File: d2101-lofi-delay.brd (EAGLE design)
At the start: 100 x 50 mm, 65 parts, among them U3 FX2-20P-1.27DS, U4 FX2-20S-1.27DS

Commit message: D2101 done
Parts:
- removed C10, C11, C8, C9: 100N, capacitors:C-0805
- removed C12: 100N(FILM), capacitors:C050-025X075
- removed C13: 10N(FILM), capacitors:C050-025X075
- removed DA3, DA4: NE5532, f-opamp:SO08
- removed DA5, DA6: NJM2068M, ic-jrc:SO-8
- removed R19: 1K, resistors:R-0805
- removed R20: 20K, resistors:R-0805
- removed R21, R24, R25: 100K, resistors:R-0805
- removed R22, R23: 2*B50K*, potentiometers:RV11-DUAL
- added C23: 47U/16V, capacitors-electrolytic:E2-5
- added C27, C32, C33: 100N(FILM), capacitors:C050-025X075
- added C28, C29: 10N(FILM), capacitors:C050-025X075
- added C30, C31, C34, C35: 100N, capacitors:C-0805
- added C36, C37: 47N(FILM), capacitors:C050-025X075
- added C38, C39: 47U/35V, capacitors-electrolytic:E3,5-8
- added DD2: PT2399S, ic-princeton-technologies:SO-16
- added R29, R30, R31, R34, R35, R36, R37, R38, R39: 10K, resistors:R-0805
- added R32, R33: 15K, resistors:R-0805
- added R40, R42: 2*B50K*, potentiometers:RV11-DUAL
- added R41, R43, R44, R45: 1K, resistors:R-0805
- added SA2: 108-0051-EVX, switches:108-0051-EVX
- added VD1, VD2, VD3, VD4: BAV199, diodes:SOT23
- C16, C17: value 2N2(FILM) -> 10N(FILM)
- C19: value 47U/16V -> 100N; device capacitors-electrolytic:E2-5 -> capacitors:C-0805
- C20, C21: value 100N -> 2N2(FILM); device capacitors:C-0805 -> capacitors:C050-025X075
- C22: value 10N(FILM) -> 47U/16V; device capacitors:C050-025X075 -> capacitors-electrolytic:E2-5
- C24: value 47N(FILM) -> 2N2(FILM)
- C25: value 10U/35V -> 2N2(FILM); device capacitors-electrolytic:E2-5 -> capacitors:C050-025X075
- C26: value 22P -> 100N(FILM); device capacitors:C-0805 -> capacitors:C050-025X075
- DA1: value NE5532 -> NJM78L05UA; device f-opamp:SO08 -> regulators-linear:SOT89
- DA2: value NCP1117ST50T3G -> NJM2068M; device regulators-linear:SOT223 -> ic-jrc:SO-8
- R1: value 100K -> 10K
- R10: value 22K -> 10K
- R12, R14: value 10K -> 10R(1206); device resistors:R-0805 -> resistors:R-1206
- R13: value 1K -> 10R(1206); device resistors:R-0805 -> resistors:R-1206
- R15, R16: value 10K -> 15K
- R17: value 10K -> 1K
- R18: value 15K -> 1K
- R2: value 2*B20K(CD) -> 10K; device potentiometers:RV11-DUAL -> resistors:R-0805
- R26, R27: value 10K -> 100K
- R5: value 100K -> 2*B20K(CD); device resistors:R-0805 -> potentiometers:RV11-DUAL
- R6, R7, R8: value 10R(1206) -> 10K; device resistors:R-1206 -> resistors:R-0805
- R9: value 15K -> 10K
- SA1: value 108-0051-EVX -> 108-0052-EVX; device switches:108-0051-EVX -> switches:108-0052-EVX
- moved R28 353.6 mm to (50.5, 23.0), turned to 90 degrees
- moved C3 347.6 mm to (8.00, 29.8), turned to 90 degrees
- moved R26 347.2 mm to (48.0, 23.0), turned to 270 degrees
- moved R9 344.0 mm to (24.5, 22.0), turned to 90 degrees
- moved R27 339.8 mm to (45.5, 13.0), turned to 270 degrees
- moved R2 337.4 mm to (27.0, 13.0)
- moved R4 330.5 mm to (27.0, 18.0)
- moved SA1 329.1 mm to (17.0, 37.0), turned to 180 degrees
- moved C26 326.7 mm to (58.0, 30.0), turned to 180 degrees
- moved R3 325.6 mm to (27.0, 15.5), turned to 180 degrees
- moved C24 309.6 mm to (58.0, 27.0), turned to 180 degrees
- moved C22 303.0 mm to (71.0, 26.0)
- moved C25 302.8 mm to (58.0, 15.0)
- moved R18 289.7 mm to (34.0, 32.0)
- moved R14 282.7 mm to (35.0, 36.0), turned to 180 degrees
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- renumbered U3 to U1, U4 to U2
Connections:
- removed net N$12: C25.-, R20.1, R24.2
- removed net N$26: R1.1
- removed net N$27: R22.2'
- removed net N$29: C3.2, DA6.1, R9.2
- removed net N$66: R13.1, SA1.2
- removed net V+: DA5.8, DA6.8
- removed net V-: DA5.4, DA6.4
- new net FBK_INT_LEFT: C3.2, DA2.1, PCB1.BOUTL', R15.2, SA1.4
- new net FBK_INT_RIGHT: C4.2, DA2.7, PCB1.BOUTR', R16.2, SA1.1
- new net FBK_LEFT: PCB1.ALFBK, PCB1.ALFBK', SA1.6
- new net FBK_RIGHT: PCB1.ARFBK, PCB1.ARFBK', SA1.3
- new net N$39: DA2.5, R11.2, R8.2
- new net N$40: R10.2, R11.1, R5.1'
- new net N$48: C28.2, R34.2, R36.2, R38.2
- new net N$49: C20.1, DD1.16, R30.1
- new net N$50: C20.2, DD1.15, R32.1
- new net N$51: C24.1, DD1.14, R34.1, R44.1
- new net N$52: C24.2, DD1.13, R36.1
- new net N$53: C26.1, DD1.12, R38.1
- new net N$54: C26.2, DD1.11
- new net N$55: C32.1, DD1.10
- new net N$56: C32.2, DD1.9
- new net N$57: C36.2, C38.+, R44.2
- new net N$58: C30.2, DD1.7
- new net N$59: C34.2, DD1.8
- new net N$60: DD1.6, R41.2
- new net N$62: C14.2, R26.2, R28.1
- new net N$63: C16.2, R28.2, R30.2, R32.2
- new net N$69: C22.+, DD1.2
- new net OUT_LEFT: C39.-, R10.1
- new net OUT_RIGHT: C38.-, R3.1
- net +15V: now also DA2.8, R13.2; no longer C10.2, C8.2, DA1.8, DA3.8, DA4.8, R6.2
- net +5V: now also C19.2, DA1.1, DD2.1; no longer DA2.2, DA2.4
- net -15V: now also DA2.4, R14.2; no longer C11.1, C9.1, DA1.4, DA3.4, DA4.4, R8.2
- net GND: now also C16.1, C17.1, C19.1, C22.-, C23.-, C28.1, C29.1, C30.1, C31.1, C34.1, C35.1, C36.1, C37.1, DA1.2, DA1.2@1, DD2.3, DD2.4, R26.1, R27.1, R40.2, R40.3, R42.2, R42.2', R42.3, R42.3', R5.2, R5.2', R6.1, R9.1, VD1.1, VD2.2, VD3.1, VD4.2; no longer C10.1, C11.2, C13.1, C19.-, C20.1, C21.1, C22.1, C24.1, C8.1, C9.2, DA2.1, DA5.3, DA5.5, R2.2, R22.1', R22.2, R22.3, R23.2', R23.3', R24.1, R25.1, R3.1
- net N$1: now also R42.1, R43.1; no longer PCB1.ALFBK, PCB1.ALFBK'
- net N$10: now also C17.2, R29.2, R31.2, R33.2; no longer C13.2, R12.2, R14.2, R18.2
- net N$11: now also PCB1.BINL, R1.1; no longer R28.1
- net N$13: now also R18.1, SA1.2; no longer C26.1, DA5.6, R20.2, R21.1
- net N$14: now also R42.1', SA2.3; no longer R23.1', SA1.3
- net N$15: now also C29.2, R35.2, R37.2, R39.2; no longer C22.2, R15.2, R16.2, R17.2
- net N$17: now also C21.2, DD2.15, R33.1; no longer C16.2, DD1.15, R18.1
- net N$18: now also C25.1, DD2.14, R35.1, R45.1; no longer C17.1, DD1.14, R15.1, R19.1
- net N$19: now also C25.2, DD2.13, R37.1; no longer C17.2, DD1.13, R16.1
- net N$2: now also R41.1, SA2.2; no longer PCB1.ARFBK, PCB1.ARFBK'
- net N$20: now also C27.1, DD2.12, R39.1; no longer C14.1, DD1.12, R17.1
- net N$21: now also C27.2, DD2.11; no longer C14.2, DD1.11
- net N$22: now also C33.1, DD2.10; no longer C15.1, DD1.10
- net N$23: now also C33.2, DD2.9; no longer C15.2, DD1.9
- net N$24: now also C37.2, C39.+, R45.2; no longer C24.2, C25.+, R19.2
- net N$25: now also C4.1, DA2.6, R16.1, R9.2; no longer R5.1
- net N$28: now also PCB1.BINR, R7.1; no longer R4.1
- net N$3: now also C15.1, R17.2, VD1.2, VD2.1; no longer C4.1, DA5.2, R1.2, R10.1, R5.2
- net N$30: now also R1.2, R2.1, R5.3; no longer R2.3, R26.1, R4.2
- net N$31: now also C31.2, DD2.7; no longer C20.2, DD1.7
- net N$32: now also C35.2, DD2.8; no longer C21.2, DD1.8
- net N$33: now also DD2.6, R43.2; no longer DD1.6, R13.2
- net N$36: now also R14.1; no longer R8.1
- net N$37: now also C23.+, DD2.2; no longer C19.+, DD1.2
- net N$4: now also C21.1, DD2.16, R31.1; no longer C16.1, DD1.16, R14.1
- net N$44: now also DA1.3, R12.2; no longer DA2.3, R7.2
- net N$5: now also C14.1, R18.2, VD3.2, VD4.1; no longer C4.2, DA5.1, R10.2, R11.1
- net N$6: now also R17.1, SA1.5; no longer C12.1, R11.2
- net N$61: now also DA2.3, R2.2, R4.2; no longer DA6.3, R26.2, R27.2
- net N$64: now also DA2.2, R15.1, R6.2; no longer DA6.2, R3.2, R9.1
- net N$65: now also R3.2, R4.1, R5.1; no longer R2.1, R27.1, R28.2
- net N$7: now also R5.3', R7.2, R8.1; no longer C26.2, DA5.7, R21.2, R22.3'
- net N$8: now also R40.1, SA2.1; no longer R22.1, SA1.1
- net N$9: now also C15.2, R27.2, R29.1; no longer C12.2, R12.1, R25.2
- net P+15V: now also R12.1, R13.1; no longer R6.1, R7.1
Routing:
- net FBK_INT_RIGHT: track 0.00 -> 82.4 mm
- net N$44: track 0.00 -> 79.0 mm
- net +5V: track 0.00 -> 73.3 mm
- net FBK_LEFT: track 0.00 -> 72.5 mm
- net FBK_INT_LEFT: track 0.00 -> 63.3 mm
- net FBK_RIGHT: track 0.00 -> 58.1 mm
- net -15V: track 0.00 -> 53.3 mm
- net P+15V: track 0.00 -> 48.7 mm
- net N$16: track 0.00 -> 46.9 mm
- net N$36: track 0.00 -> 43.4 mm
- net OUT_LEFT: track 0.00 -> 41.4 mm
- net N$39: track 0.00 -> 40.7 mm, vias 0 -> 3
- net +15V: track 0.00 -> 38.8 mm, vias 0 -> 1
- net N$24: track 0.00 -> 35.9 mm
- net N$28: track 0.00 -> 33.0 mm
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
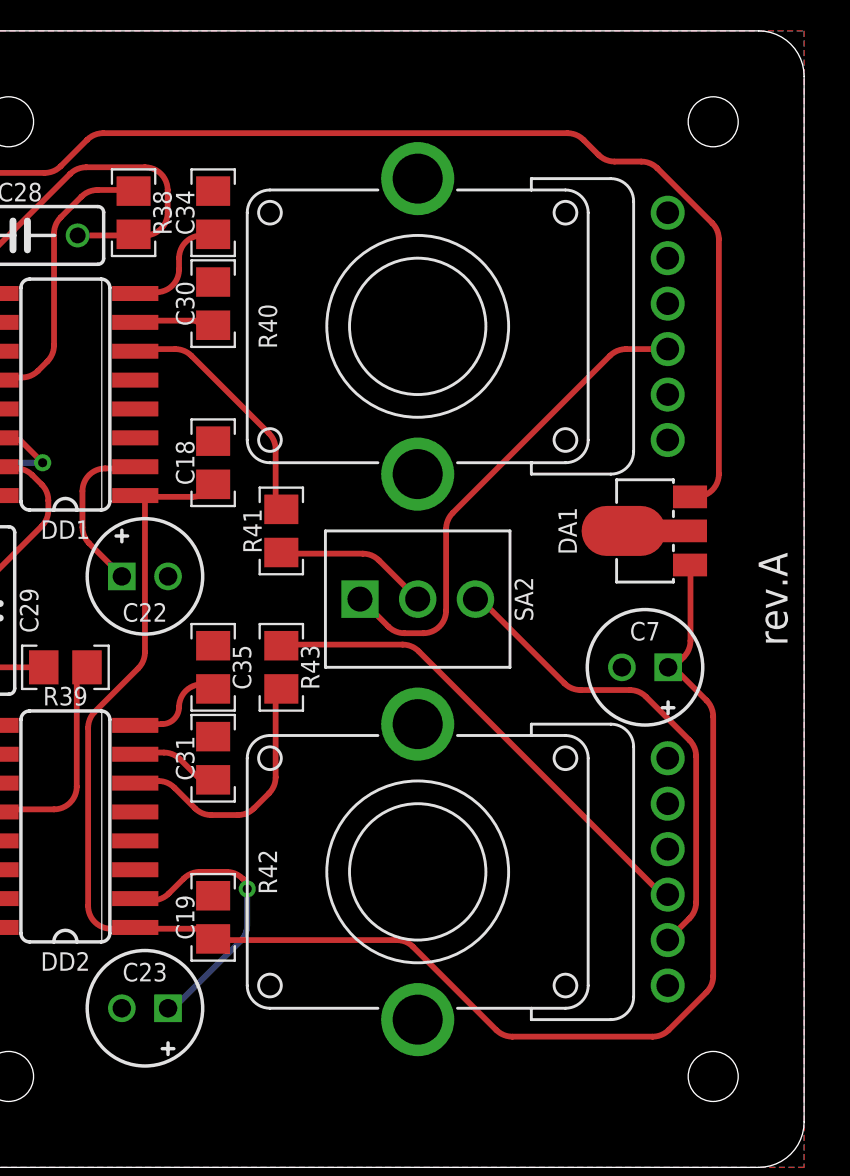
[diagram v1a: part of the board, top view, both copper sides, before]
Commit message: Replace switchable delay potentiometers with single ones
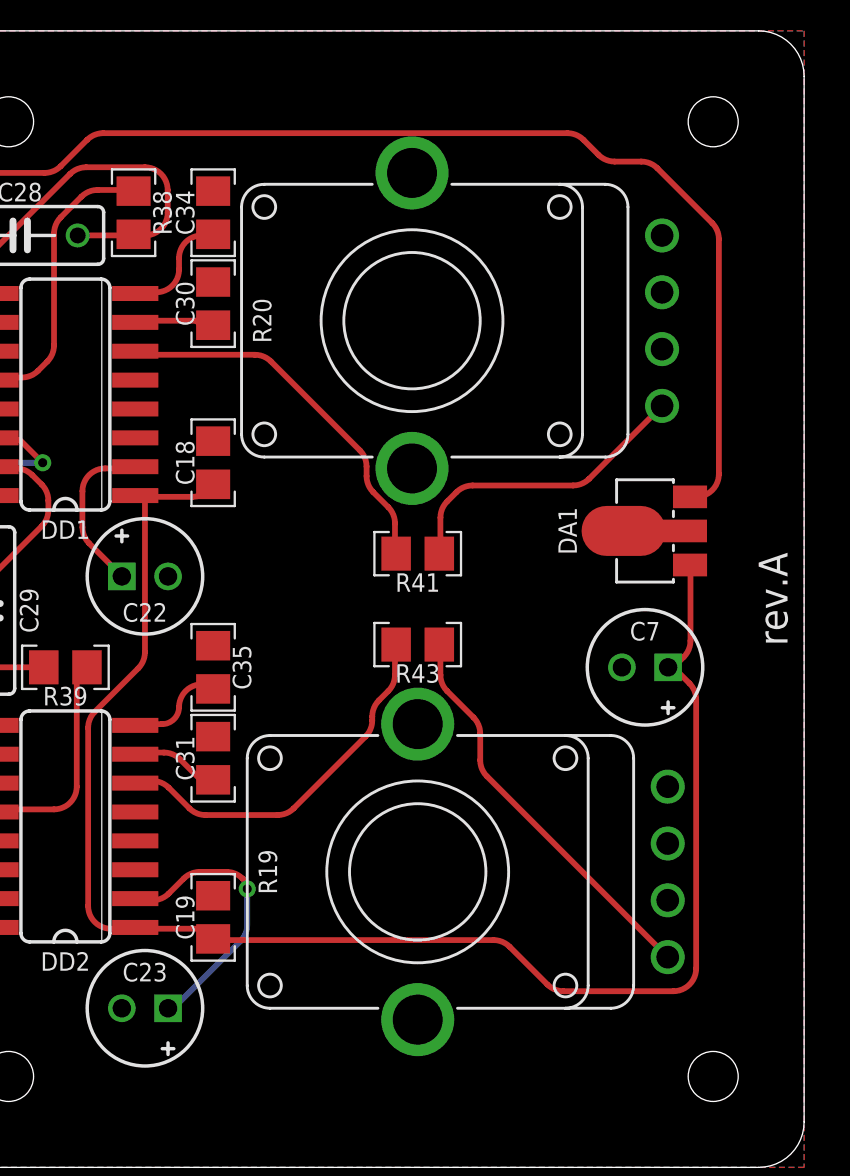
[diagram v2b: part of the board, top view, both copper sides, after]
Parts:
- removed R40, R42: 2*B50K*, potentiometers:RV11-DUAL
- removed SA2: 108-0051-EVX, switches:108-0051-EVX
- added R19, R20: B50K**, potentiometers:RV11-SINGLE
- moved R41 6.08 mm to (83.0, 27.0), turned to 180 degrees
- moved R43 6.08 mm to (83.0, 23.0), turned to 180 degrees
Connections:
- removed net N$14: R42.1', SA2.3
- removed net N$8: R40.1, SA2.1
- net GND: now also R19.2, R19.3, R20.2, R20.3; no longer R40.2, R40.3, R42.2, R42.2', R42.3, R42.3'
- net N$1: now also R19.1; no longer R42.1
- net N$2: now also R20.1; no longer SA2.2
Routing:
- net N$8: track 21.5 -> 0.00 mm
- net N$14: track 21.2 -> 0.00 mm
- net N$2: track 6.82 -> 13.5 mm
- net N$60: track 11.3 -> 16.7 mm
- net N$33: track 11.9 -> 16.5 mm
- net N$1: track 21.5 -> 17.8 mm
- net +5V: track 73.3 -> 70.2 mm

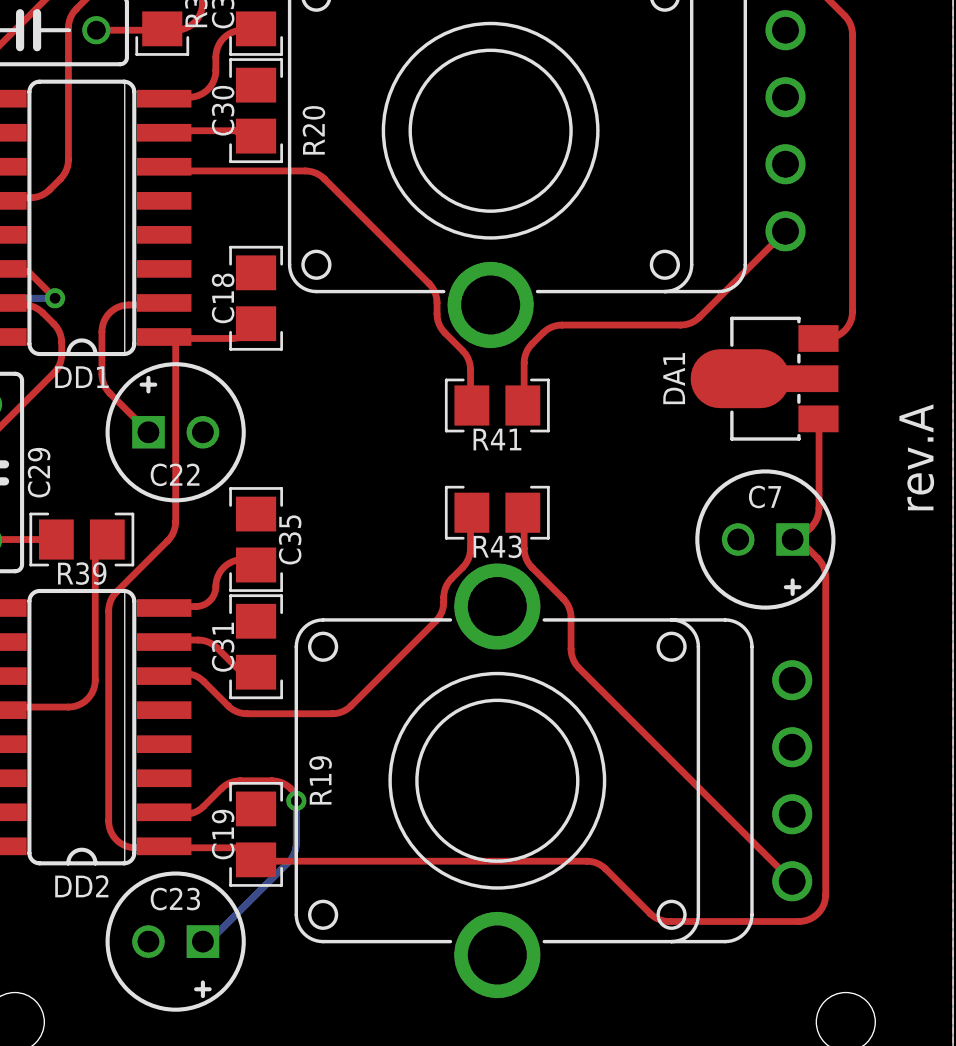
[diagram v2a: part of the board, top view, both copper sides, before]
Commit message: Minor routing adjustment
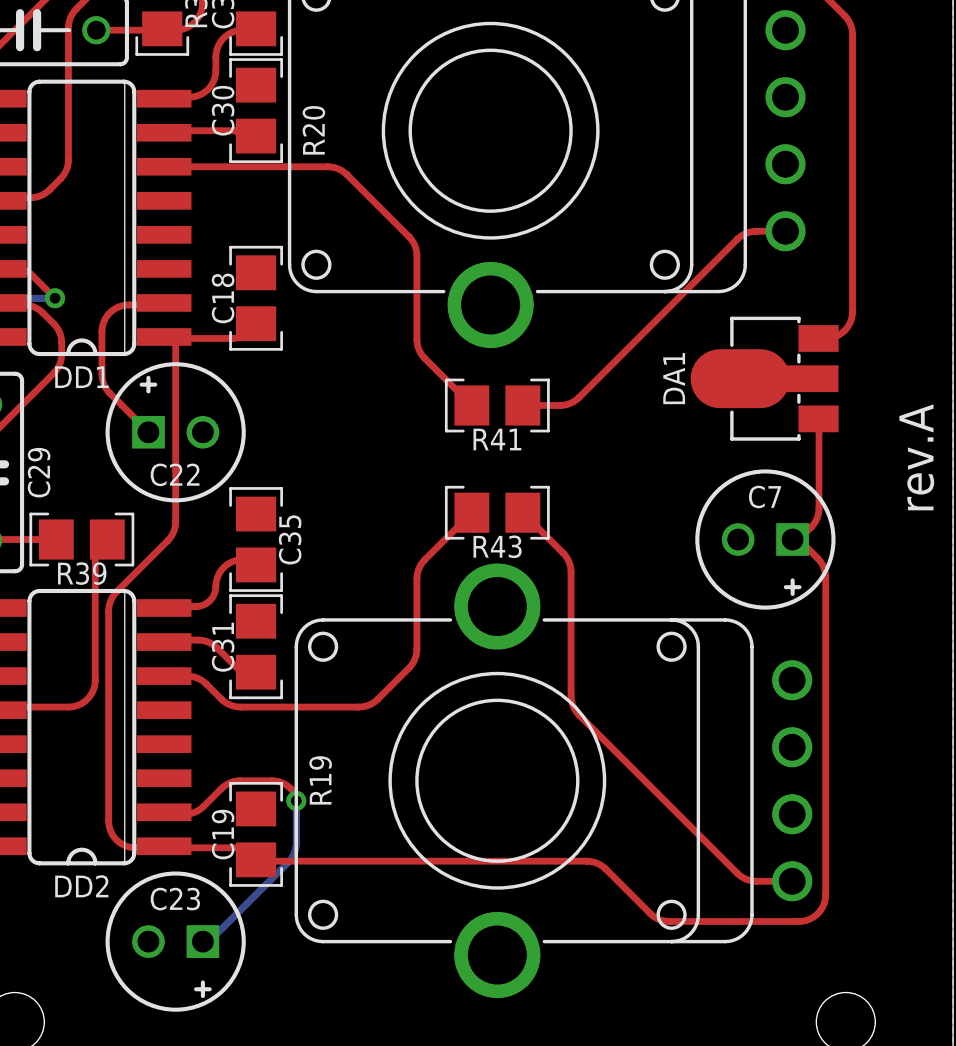
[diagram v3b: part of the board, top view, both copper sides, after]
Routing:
- net N$2: track 13.5 -> 12.4 mm
- net N$1: track 17.8 -> 18.7 mm
- net N$60: track 16.7 -> 17.3 mm
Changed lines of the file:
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@@
 <contactref element="DD2" pad="6"/>
 <contactref element="R43" pad="2"/>
-<wire x1="70.75" y1="17" x2="71.3357875" y2="17" width="0.254" layer="1"/>
-<wire x1="71.3357875" y1="17" x2="72.04289375" y2="16.70710625" width="0.254" layer="1" curve="-45"/>
-<wire x1="82" y1="23" x2="82" y2="21.6642125" width="0.254" layer="1"/>
-<wire x1="82" y1="21.6642125" x2="81.70710625" y2="20.95710625" width="0.254" layer="1" curve="-45"/>
-<wire x1="81.70710625" y1="20.95710625" x2="81.29289375" y2="20.54289375" width="0.254" layer="1"/>
-<wire x1="81.29289375" y1="20.54289375" x2="81" y2="19.8357875" width="0.254" layer="1" curve="45"/>
-<wire x1="81" y1="19.8357875" x2="81" y2="19.6642125" width="0.254" layer="1"/>
-<wire x1="81" y1="19.6642125" x2="80.70710625" y2="18.95710625" width="0.254" layer="1" curve="-45"/>
-<wire x1="80.70710625" y1="18.95710625" x2="77.54289375" y2="15.79289375" width="0.254" layer="1"/>
-<wire x1="77.54289375" y1="15.79289375" x2="76.8357875" y2="15.5" width="0.254" layer="1" curve="-45"/>
-<wire x1="76.8357875" y1="15.5" x2="73.6642125" y2="15.5" width="0.254" layer="1"/>
-<wire x1="73.6642125" y1="15.5" x2="72.95710625" y2="15.79289375" width="0.254" layer="1" curve="-45"/>
-<wire x1="72.95710625" y1="15.79289375" x2="72.04289375" y2="16.70710625" width="0.254" layer="1"/>
-<wire x1="70.75" y1="17" x2="70.5734" y2="16.905" width="0.254" layer="1"/>
-<wire x1="82" y1="23" x2="82.05" y2="23" width="0.254" layer="1"/>
+<wire x1="70.5734" y1="16.905" x2="71.4307875" y2="16.905" width="0.254" layer="1"/>
+<wire x1="71.4307875" y1="16.905" x2="72.13789375" y2="16.61210625" width="0.254" layer="1" curve="-45"/>
+<wire x1="72.13789375" y1="16.61210625" x2="72.70710625" y2="16.04289375" width="0.254" layer="1"/>
+<wire x1="72.70710625" y1="16.04289375" x2="73.4142125" y2="15.75" width="0.254" layer="1" curve="45"/>
+<wire x1="73.4142125" y1="15.75" x2="77.8357875" y2="15.75" width="0.254" layer="1"/>
+<wire x1="77.8357875" y1="15.75" x2="78.54289375" y2="16.04289375" width="0.254" layer="1" curve="45"/>
+<wire x1="78.54289375" y1="16.04289375" x2="79.70710625" y2="17.20710625" width="0.254" layer="1"/>
+<wire x1="79.70710625" y1="17.20710625" x2="80" y2="17.9142125" width="0.254" layer="1" curve="45"/>
+<wire x1="80" y1="17.9142125" x2="80" y2="20.5357875" width="0.254" layer="1"/>
+<wire x1="80" y1="20.5357875" x2="80.29289375" y2="21.24289375" width="0.254" layer="1" curve="-45"/>
+<wire x1="80.29289375" y1="21.24289375" x2="82.05" y2="23" width="0.254" layer="1"/>
 </signal>
 <signal name="N$44">
@@
 <contactref element="DD1" pad="6"/>
 <contactref element="R41" pad="2"/>
-<wire x1="82" y1="27" x2="82" y2="28.3357875" width="0.254" layer="1"/>
-<wire x1="82" y1="28.3357875" x2="81.70710625" y2="29.04289375" width="0.254" layer="1" curve="45"/>
-<wire x1="81.70710625" y1="29.04289375" x2="81.04289375" y2="29.70710625" width="0.254" layer="1"/>
-<wire x1="81.04289375" y1="29.70710625" x2="80.75" y2="30.4142125" width="0.254" layer="1" curve="-45"/>
-<wire x1="80.75" y1="30.4142125" x2="80.75" y2="30.8357875" width="0.254" layer="1"/>
-<wire x1="80.75" y1="30.8357875" x2="80.45710625" y2="31.54289375" width="0.254" layer="1" curve="45"/>
-<wire x1="80.45710625" y1="31.54289375" x2="76.54289375" y2="35.45710625" width="0.254" layer="1"/>
-<wire x1="76.54289375" y1="35.45710625" x2="75.8357875" y2="35.75" width="0.254" layer="1" curve="45"/>
-<wire x1="75.8357875" y1="35.75" x2="71.5" y2="35.75" width="0.254" layer="1"/>
-<wire x1="71.25" y1="36" x2="71.5" y2="35.75" width="0.254" layer="1"/>
-<wire x1="70.75" y1="36" x2="71.25" y2="36" width="0.254" layer="1"/>
-<wire x1="70.75" y1="36" x2="70.5734" y2="35.905" width="0.254" layer="1"/>
-<wire x1="82" y1="27" x2="82.05" y2="27" width="0.254" layer="1"/>
+<wire x1="70.5734" y1="35.905" x2="76.6807875" y2="35.905" width="0.254" layer="1"/>
+<wire x1="76.6807875" y1="35.905" x2="77.38789375" y2="35.61210625" width="0.254" layer="1" curve="-45"/>
+<wire x1="77.38789375" y1="35.61210625" x2="79.70710625" y2="33.29289375" width="0.254" layer="1"/>
+<wire x1="79.70710625" y1="33.29289375" x2="80" y2="32.5857875" width="0.254" layer="1" curve="-45"/>
+<wire x1="80" y1="32.5857875" x2="80" y2="29.4642125" width="0.254" layer="1"/>
+<wire x1="80" y1="29.4642125" x2="80.29289375" y2="28.75710625" width="0.254" layer="1" curve="45"/>
+<wire x1="80.29289375" y1="28.75710625" x2="82.05" y2="27" width="0.254" layer="1"/>
 </signal>
 <signal name="N$62">
@@
 <contactref element="R43" pad="1"/>
 <contactref element="R19" pad="1"/>
-<wire x1="84.29289375" y1="20.95710625" x2="85.45710625" y2="19.79289375" width="0.254" layer="1"/>
-<wire x1="85.45710625" y1="19.79289375" x2="85.75" y2="19.0857875" width="0.254" layer="1" curve="-45"/>
-<wire x1="94" y1="9.25" x2="86.04289375" y2="17.20710625" width="0.254" layer="1"/>
-<wire x1="86.04289375" y1="17.20710625" x2="85.75" y2="17.9142125" width="0.254" layer="1" curve="-45"/>
-<wire x1="85.75" y1="17.9142125" x2="85.75" y2="19.0857875" width="0.254" layer="1"/>
-<wire x1="84" y1="23" x2="84" y2="21.6642125" width="0.254" layer="1"/>
-<wire x1="84" y1="21.6642125" x2="84.29289375" y2="20.95710625" width="0.254" layer="1" curve="45"/>
-<wire x1="84" y1="23" x2="83.95" y2="23" width="0.254" layer="1"/>
+<wire x1="94" y1="9.25" x2="92.6642125" y2="9.25" width="0.254" layer="1"/>
+<wire x1="92.6642125" y1="9.25" x2="91.95710625" y2="9.54289375" width="0.254" layer="1" curve="-45"/>
+<wire x1="91.95710625" y1="9.54289375" x2="86.04289375" y2="15.45710625" width="0.254" layer="1"/>
+<wire x1="86.04289375" y1="15.45710625" x2="85.75" y2="16.1642125" width="0.254" layer="1" curve="-45"/>
+<wire x1="85.75" y1="16.1642125" x2="85.75" y2="20.7857875" width="0.254" layer="1"/>
+<wire x1="85.75" y1="20.7857875" x2="85.45710625" y2="21.49289375" width="0.254" layer="1" curve="45"/>
+<wire x1="85.45710625" y1="21.49289375" x2="83.95" y2="23" width="0.254" layer="1"/>
 </signal>
 <signal name="N$2">
 <contactref element="R41" pad="1"/>
 <contactref element="R20" pad="1"/>
-<wire x1="84.29289375" y1="29.29289375" x2="84.70710625" y2="29.70710625" width="0.254" layer="1"/>
-<wire x1="84.70710625" y1="29.70710625" x2="85.4142125" y2="30" width="0.254" layer="1" curve="-45"/>
-<wire x1="93.75" y1="33.5" x2="90.54289375" y2="30.29289375" width="0.254" layer="1"/>
-<wire x1="90.54289375" y1="30.29289375" x2="89.8357875" y2="30" width="0.254" layer="1" curve="-45"/>
-<wire x1="89.8357875" y1="30" x2="85.4142125" y2="30" width="0.254" layer="1"/>
-<wire x1="84" y1="27" x2="84" y2="28.5857875" width="0.254" layer="1"/>
-<wire x1="84" y1="28.5857875" x2="84.29289375" y2="29.29289375" width="0.254" layer="1" curve="-45"/>
-<wire x1="84" y1="27" x2="83.95" y2="27" width="0.254" layer="1"/>
+<wire x1="93.75" y1="33.5" x2="92.6642125" y2="33.5" width="0.254" layer="1"/>
+<wire x1="92.6642125" y1="33.5" x2="91.95710625" y2="33.20710625" width="0.254" layer="1" curve="45"/>
+<wire x1="91.95710625" y1="33.20710625" x2="86.04289375" y2="27.29289375" width="0.254" layer="1"/>
+<wire x1="86.04289375" y1="27.29289375" x2="85.3357875" y2="27" width="0.254" layer="1" curve="-45"/>
+<wire x1="85.3357875" y1="27" x2="83.95" y2="27" width="0.254" layer="1"/>
 </signal>
 <signal name="N$11">
